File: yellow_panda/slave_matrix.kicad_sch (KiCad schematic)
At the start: 64 parts

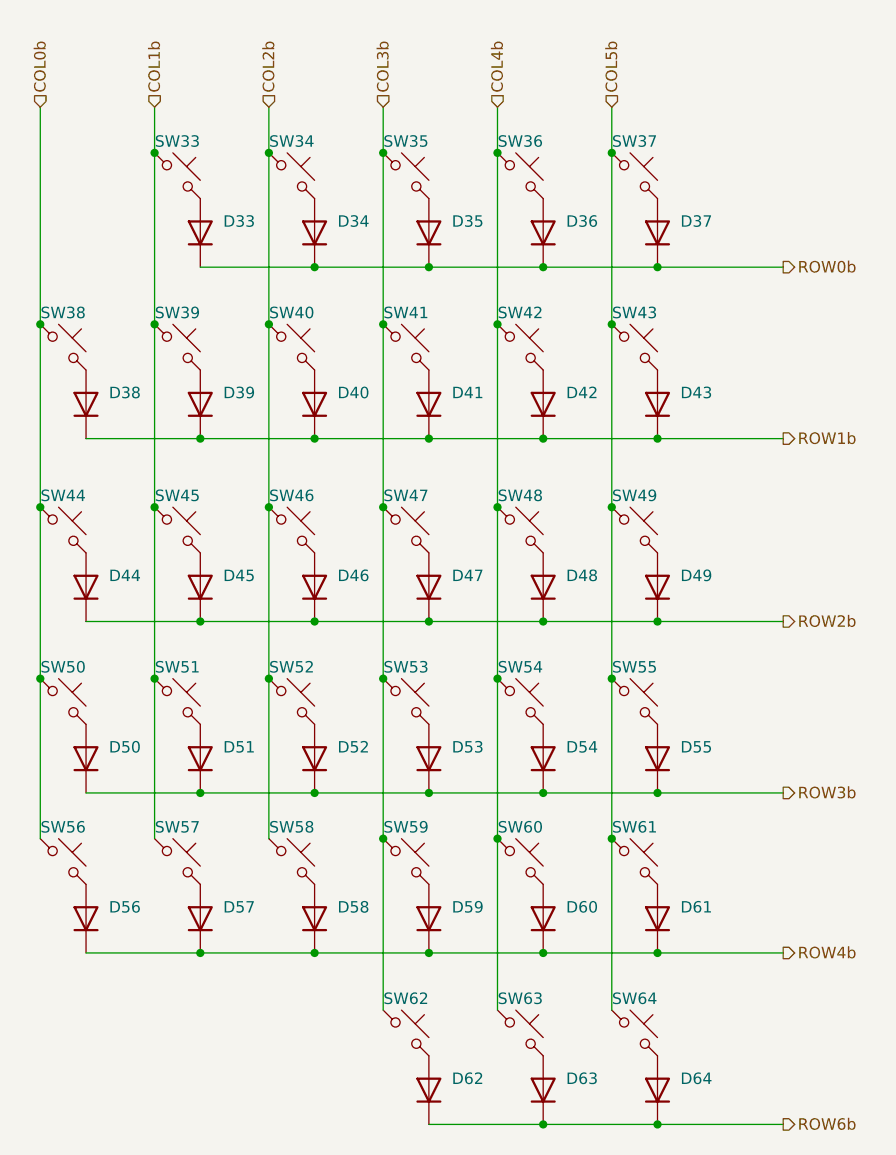
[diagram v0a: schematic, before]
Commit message: Everything is in place now
Swap STM MCU, Correct Switches,
add diodes, caps and resistors
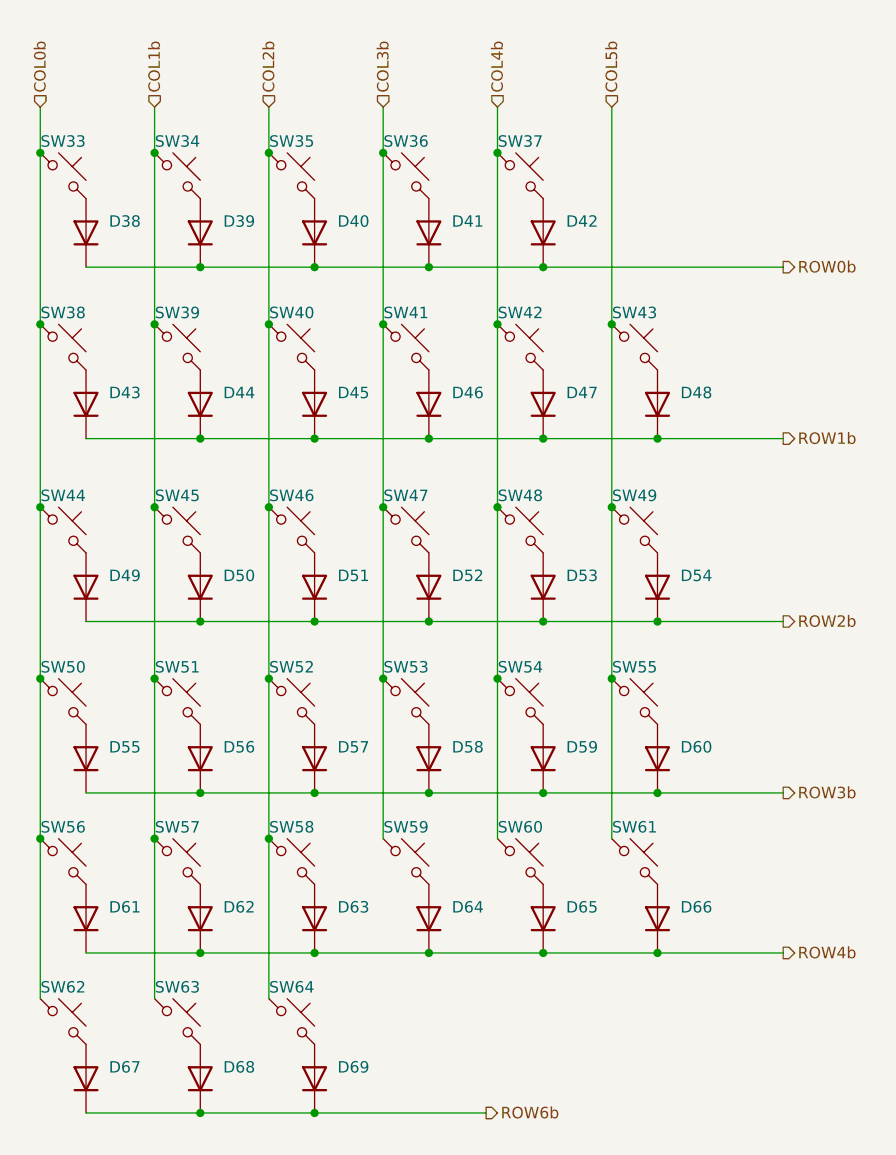
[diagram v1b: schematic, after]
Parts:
- SW33, SW34, SW35, SW36, SW37, SW38, SW39, SW40, SW41, SW42, SW43, SW44, SW45, SW46, SW47, SW48, SW49, SW50, SW51, SW52, SW53, SW54, SW55, SW56, SW57, SW58, SW59, SW60, SW61, SW63, SW64: footprint kiswitch/hotswaps:SW_Hotswap_Kailh_Choc_V1_Plated_1.00u -> PCM_Switch_Keyboard_Hotswap_Kailh:SW_Hotswap_Kailh_Choc_V1_Plated_1.00u
- SW62: footprint kiswitch/hotswaps:SW_Hotswap_Kailh_Choc_V1_Plated_1.00u -> PCM_Switch_Keyboard_Hotswap_Kailh:SW_Hotswap_Kailh_Choc_V1_Plated_1.50u
- renumbered D33 to D38, D34 to D39, D35 to D40, D36 to D41, D37 to D42, D38 to D43, D39 to D44, D40 to D45, D41 to D46, D42 to D47, D43 to D48, D44 to D49, D45 to D50, D46 to D51, D47 to D52, D48 to D53, D49 to D54, D50 to D55, D51 to D56, D52 to D57, D53 to D58, D54 to D59, D55 to D60, D56 to D61, D57 to D62, D58 to D63, D59 to D64, D60 to D65, D61 to D66, D62 to D67, D63 to D68, D64 to D69
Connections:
- net COL0b: now also SW33.1, SW62.1
- net COL1b: now also SW34.1, SW63.1; no longer SW33.1
- net COL2b: now also SW35.1, SW64.1; no longer SW34.1
- net COL3b: now also SW36.1; no longer SW35.1, SW62.1
- net COL4b: now also SW37.1; no longer SW36.1, SW63.1
- net COL5b: no longer SW37.1, SW64.1
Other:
- moved on the sheet: D38, D39, D40, D41, D42, D67, D68, D69, SW33, SW34, SW35, SW36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

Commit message: Finished the design
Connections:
- net COL0b: now also SW43.1, SW49.1, SW55.1, SW61.1; no longer SW33.1, SW38.1, SW44.1, SW50.1, SW56.1, SW62.1
- net COL1b: now also SW37.1, SW42.1, SW48.1, SW54.1, SW60.1; no longer SW34.1, SW39.1, SW45.1, SW51.1, SW57.1, SW63.1
- net COL2b: now also SW36.1, SW41.1, SW47.1, SW53.1, SW59.1; no longer SW35.1, SW40.1, SW46.1, SW52.1, SW58.1, SW64.1
- net COL3b: now also SW35.1, SW40.1, SW46.1, SW52.1, SW58.1, SW64.1; no longer SW36.1, SW41.1, SW47.1, SW53.1, SW59.1
- net COL4b: now also SW34.1, SW39.1, SW45.1, SW51.1, SW57.1, SW63.1; no longer SW37.1, SW42.1, SW48.1, SW54.1, SW60.1
- net COL5b: now also SW33.1, SW38.1, SW44.1, SW50.1, SW56.1, SW62.1; no longer SW43.1, SW49.1, SW55.1, SW61.1
- net ROW6b renamed ROW5b
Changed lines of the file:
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@@
 		)
 	)
-	(hierarchical_label "COL5b"
+	(global_label "COL1b"
+		(shape input)
+		(at 154.94 34.29 90)
+		(fields_autoplaced yes)
+		(effects
+			(font
+				(size 1.27 1.27)
+			)
+			(justify left)
+		)
+		(property "Intersheetrefs" "${INTERSHEET_REFS}"
+			(at 154.94 25.3177 90)
+			(effects
+				(font
+					(size 1.27 1.27)
+				)
+				(justify left)
+				(hide yes)
+			)
+		)
+	)
+	(global_label "ROW0b"
+		(shape output)
+		(at 186.69 52.07 0)
+		(fields_autoplaced yes)
+		(effects
+			(font
+				(size 1.27 1.27)
+			)
+			(justify left)
+		)
+		(property "Intersheetrefs" "${INTERSHEET_REFS}"
+			(at 196.0856 52.07 0)
+			(effects
+				(font
+					(size 1.27 1.27)
+				)
+				(justify left)
+				(hide yes)
+			)
+		)
+	)
+	(global_label "ROW1b"
+		(shape output)
+		(at 186.69 71.12 0)
+		(fields_autoplaced yes)
+		(effects
+			(font
+				(size 1.27 1.27)
+			)
+			(justify left)
+		)
+		(property "Intersheetrefs" "${INTERSHEET_REFS}"
+			(at 196.0856 71.12 0)
+			(effects
+				(font
+					(size 1.27 1.27)
+				)
+				(justify left)
+				(hide yes)
+			)
+		)
+	)
+	(global_label "ROW4b"
+		(shape output)
+		(at 186.69 128.27 0)
+		(fields_autoplaced yes)
+		(effects
+			(font
+				(size 1.27 1.27)
+			)
+			(justify left)
+		)
+		(property "Intersheetrefs" "${INTERSHEET_REFS}"
+			(at 196.0856 128.27 0)
+			(effects
+				(font
+					(size 1.27 1.27)
+				)
+				(justify left)
+				(hide yes)
+			)
+		)
+	)
+	(global_label "COL4b"
+		(shape input)
+		(at 116.84 34.29 90)
+		(fields_autoplaced yes)
+		(effects
+			(font
+				(size 1.27 1.27)
+			)
+			(justify left)
+		)
+		(property "Intersheetrefs" "${INTERSHEET_REFS}"
+			(at 116.84 25.3177 90)
+			(effects
+				(font
+					(size 1.27 1.27)
+				)
+				(justify left)
+				(hide yes)
+			)
+		)
+	)
+	(global_label "COL2b"
+		(shape input)
+		(at 142.24 34.29 90)
+		(fields_autoplaced yes)
+		(effects
+			(font
+				(size 1.27 1.27)
+			)
+			(justify left)
+		)
+		(property "Intersheetrefs" "${INTERSHEET_REFS}"
+			(at 142.24 25.3177 90)
+			(effects
+				(font
+					(size 1.27 1.27)
+				)
+				(justify left)
+				(hide yes)
+			)
+		)
+	)
+	(global_label "ROW2b"
+		(shape output)
+		(at 186.69 91.44 0)
+		(fields_autoplaced yes)
+		(effects
+			(font
+				(size 1.27 1.27)
+			)
+			(justify left)
+		)
+		(property "Intersheetrefs" "${INTERSHEET_REFS}"
+			(at 196.0856 91.44 0)
+			(effects
+				(font
+					(size 1.27 1.27)
+				)
+				(justify left)
+				(hide yes)
+			)
+		)
+	)
+	(global_label "ROW5b"
+		(shape output)
+		(at 153.67 146.05 0)
+		(fields_autoplaced yes)
+		(effects
+			(font
+				(size 1.27 1.27)
+			)
+			(justify left)
+		)
+		(property "Intersheetrefs" "${INTERSHEET_REFS}"
+			(at 163.0656 146.05 0)
+			(effects
+				(font
+					(size 1.27 1.27)
+				)
+				(justify left)
+				(hide yes)
+			)
+		)
+	)
+	(global_label "COL3b"
+		(shape input)
+		(at 129.54 34.29 90)
+		(fields_autoplaced yes)
+		(effects
+			(font
+				(size 1.27 1.27)
+			)
+			(justify left)
+		)
+		(property "Intersheetrefs" "${INTERSHEET_REFS}"
+			(at 129.54 25.3177 90)
+			(effects
+				(font
+					(size 1.27 1.27)
+				)
+				(justify left)
+				(hide yes)
+			)
+		)
+	)
+	(global_label "ROW3b"
+		(shape output)
+		(at 186.69 110.49 0)
+		(fields_autoplaced yes)
+		(effects
+			(font
+				(size 1.27 1.27)
+			)
+			(justify left)
+		)
+		(property "Intersheetrefs" "${INTERSHEET_REFS}"
+			(at 196.0856 110.49 0)
+			(effects
+				(font
+					(size 1.27 1.27)
+				)
+				(justify left)
+				(hide yes)
+			)
+		)
+	)
+	(global_label "COL0b"
 		(shape input)
 		(at 167.64 34.29 90)
-		(effects
-			(font
-				(size 1.27 1.27)
-			)
-			(justify left)
-		)
-	)
-	(hierarchical_label "COL3b"
-		(shape input)
-		(at 142.24 34.29 90)
-		(effects
-			(font
-				(size 1.27 1.27)
-			)
-			(justify left)
-		)
-	)
-	(hierarchical_label "ROW4b"
-		(shape output)
-		(at 186.69 128.27 0)
-		(effects
-			(font
-				(size 1.27 1.27)
-			)
-			(justify left)
-		)
-	)
-	(hierarchical_label "COL4b"
-		(shape input)
-		(at 154.94 34.29 90)
-		(effects
-			(font
-				(size 1.27 1.27)
-			)
-			(justify left)
-		)
-	)
-	(hierarchical_label "ROW1b"
-		(shape output)
-		(at 186.69 71.12 0)
-		(effects
-			(font
-				(size 1.27 1.27)
-			)
-			(justify left)
-		)
-	)
-	(hierarchical_label "ROW3b"
-		(shape output)
-		(at 186.69 110.49 0)
-		(effects
-			(font
-				(size 1.27 1.27)
-			)
-			(justify left)
-		)
-	)
-	(hierarchical_label "ROW2b"
-		(shape output)
-		(at 186.69 91.44 0)
-		(effects
-			(font
-				(size 1.27 1.27)
-			)
-			(justify left)
-		)
-	)
-	(hierarchical_label "COL1b"
-		(shape input)
-		(at 116.84 34.29 90)
-		(effects
-			(font
-				(size 1.27 1.27)
-			)
-			(justify left)
-		)
-	)
-	(hierarchical_label "COL0b"
+		(fields_autoplaced yes)
+		(effects
+			(font
+				(size 1.27 1.27)
+			)
+			(justify left)
+		)
+		(property "Intersheetrefs" "${INTERSHEET_REFS}"
+			(at 167.64 25.3177 90)
+			(effects
+				(font
+					(size 1.27 1.27)
+				)
+				(justify left)
+				(hide yes)
+			)
+		)
+	)
+	(global_label "COL5b"
 		(shape input)
 		(at 104.14 34.29 90)
-		(effects
-			(font
-				(size 1.27 1.27)
-			)
-			(justify left)
-		)
-	)
-	(hierarchical_label "COL2b"
-		(shape input)
-		(at 129.54 34.29 90)
-		(effects
-			(font
-				(size 1.27 1.27)
-			)
-			(justify left)
-		)
-	)
-	(hierarchical_label "ROW0b"
-		(shape output)
-		(at 186.69 52.07 0)
-		(effects
-			(font
-				(size 1.27 1.27)
-			)
-			(justify left)
-		)
-	)
-	(hierarchical_label "ROW6b"
-		(shape output)
-		(at 153.67 146.05 0)
-		(effects
-			(font
-				(size 1.27 1.27)
-			)
-			(justify left)
-		)
-	)
+		(fields_autoplaced yes)
+		(effects
+			(font
+				(size 1.27 1.27)
+			)
+			(justify left)
+		)
+		(property "Intersheetrefs" "${INTERSHEET_REFS}"
+			(at 104.14 25.3177 90)
+			(effects
+				(font
+					(size 1.27 1.27)
+				)
+				(justify left)
+				(hide yes)
+			)
+		)
+	)

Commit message: v0.1b
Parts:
- D38, D39, D40, D41, D42, D43, D44, D45, D46, D47, D48, D49, D50, D51, D52, D53, D54, D55, D56, D57, D58, D59, D60, D61, D62, D63, D64, D65, D66, D67, D68, D69, SW33, SW34, SW35, SW36, SW37, SW38, SW39, SW40, SW41, SW42, SW43, SW44, SW45, SW46, SW47, SW48, SW49, SW50, SW51, SW52, SW53, SW54, SW55, SW56, SW57, SW58, SW59, SW60, SW61, SW62, SW63, SW64: value ~ -> 1N4148W; LCSC (none) -> C917030; LCSC Part (none) -> C917030
